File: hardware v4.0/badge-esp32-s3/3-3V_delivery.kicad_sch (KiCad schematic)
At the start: 24 parts, among them Q4 HL2301A, Q7 AO3424, U2 TPS630701RNMR, U8 TLV75733PDBVR

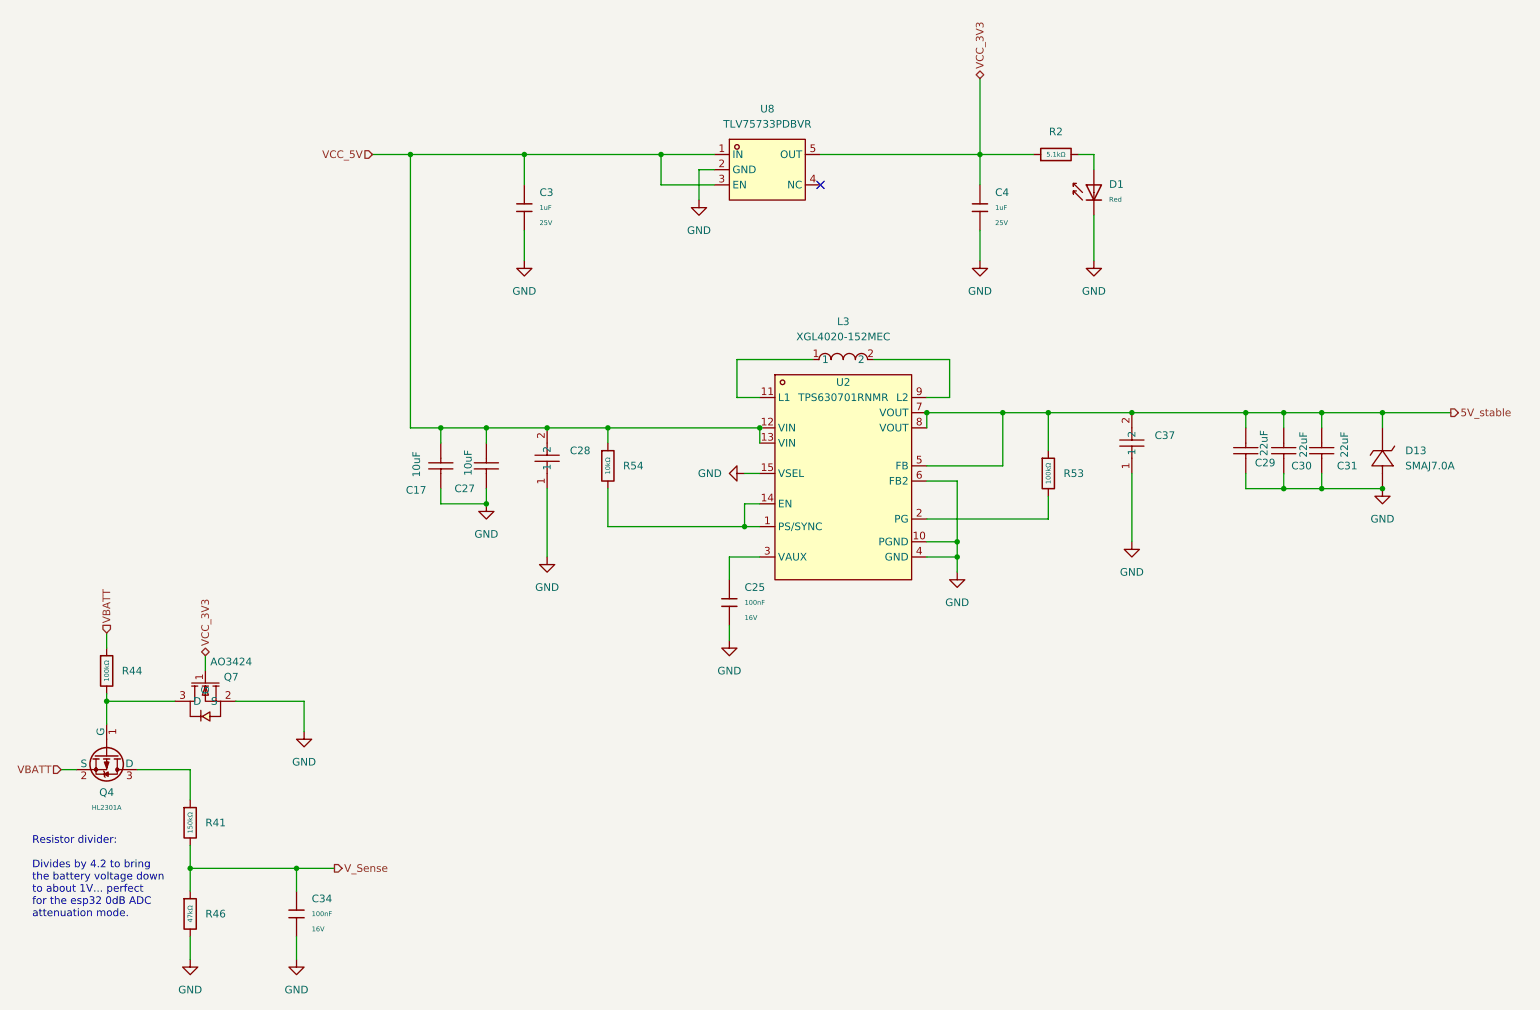
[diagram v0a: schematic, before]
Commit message: added DRD, 3.3V switching reg, and VIN
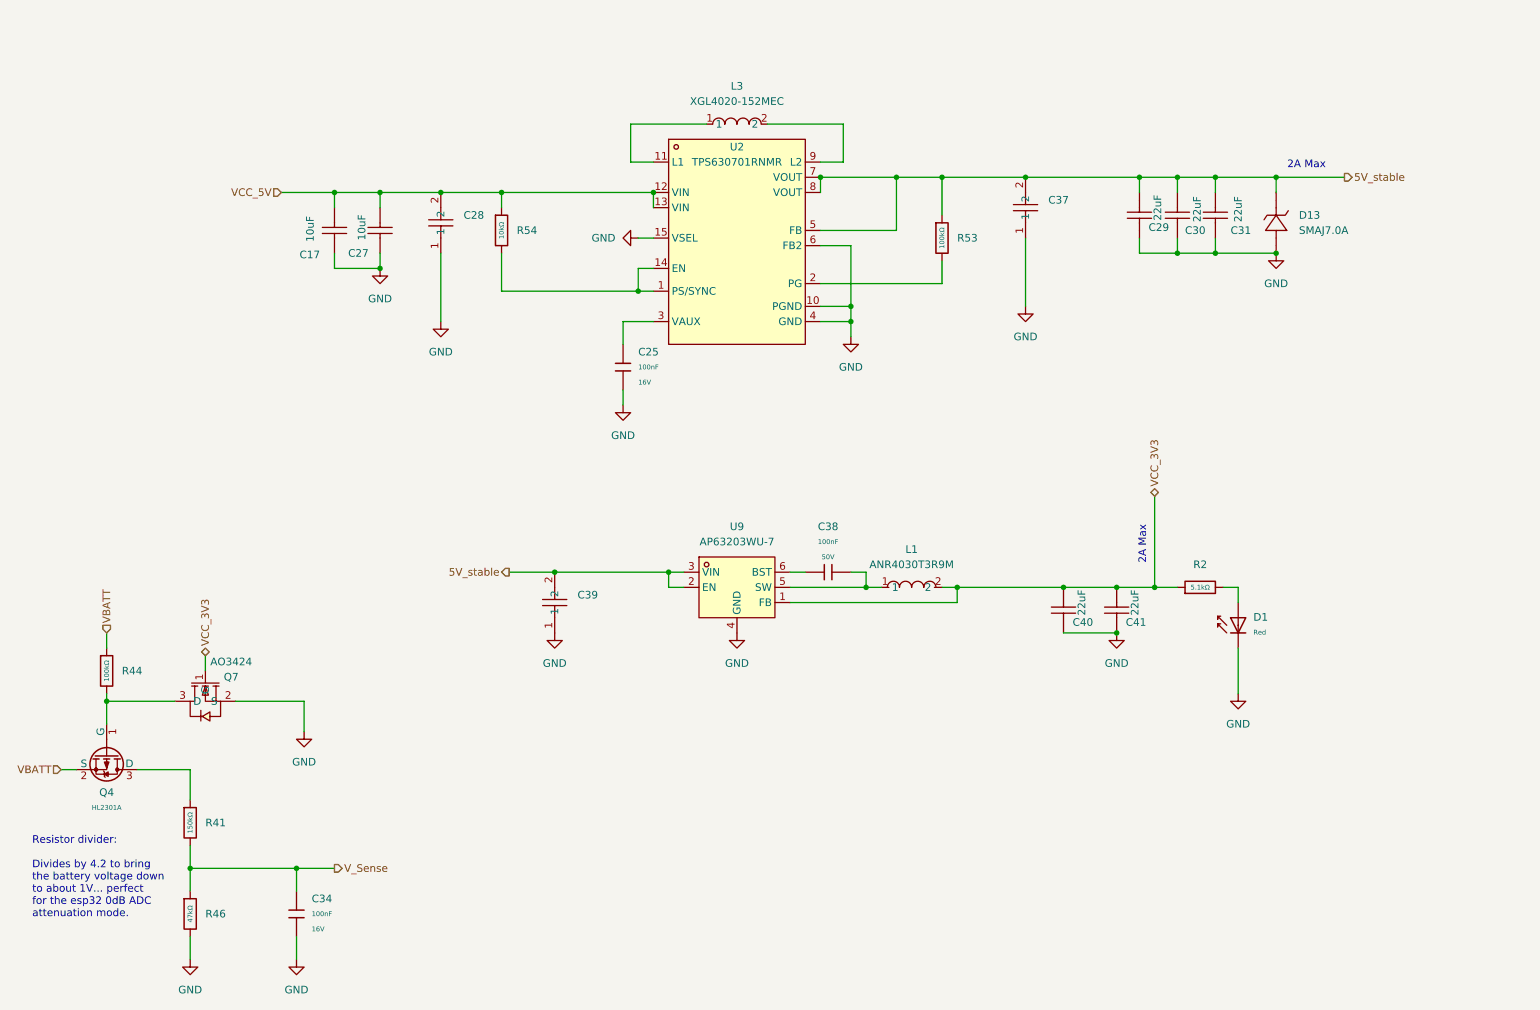
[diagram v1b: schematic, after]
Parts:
- removed C3, C4: 1uF, PCM_JLCPCB:C_0402, symbol PCM_JLCPCB-Capacitors:0402,1uF
- removed U8: TLV75733PDBVR, lcsc-lib:SOT-23-5_L2.9-W1.6-P0.95-LS2.8-BL, symbol lcsc-lib:TLV75733PDBVR
- added C38: 100nF, PCM_JLCPCB:C_0603, symbol PCM_JLCPCB-Capacitors:0603,100nF
- added C39: TMK107BBJ106MA-T, lcsc-lib:C0603, symbol lcsc-lib:TMK107BBJ106MA-T
- added C40, C41: 22uF, lcsc-lib:C0805, symbol lcsc-lib:EMK212BBJ226MG-T
- added L1: ANR4030T3R9M, lcsc-lib:IND-SMD_L4.0-W4.0, symbol lcsc-lib:ANR4030T3R9M
- added U9: AP63203WU-7, lcsc-lib:TSOT-26_L2.9-W1.6-P0.95-LS2.8-BL, symbol lcsc-lib:AP63203WU-7
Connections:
- net 5V_stable: now also C39.2, U9.2 (EN), U9.3 (VIN)
- net GND: now also C39.1, C40.1, C41.1, U9.4 (GND)
- net VCC_3V3: now also C40.2, C41.2, L1.2, U9.1 (FB)
- new net: C38.2, L1.1, U9.5 (SW)
- new net: C38.1, U9.6 (BST)
- no-connect marks 1 -> 0
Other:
- note added: "2A Max"
- moved on the sheet: C17, C25, C27, C28, C29, C30, C31, C37, D1, D13, L3, R2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
